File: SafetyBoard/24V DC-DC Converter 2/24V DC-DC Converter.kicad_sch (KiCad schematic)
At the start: 15 parts, among them J18 614004135023, U10 OKX-T/5-D12N-C

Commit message: hopefully this lets avadi pull
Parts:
- added C20: 1u, Capacitor_SMD:C_0805_2012Metric, symbol Device:C
- renumbered C27 to C16, C28 to C17, C18 to C21, C19 to C22, C29 to C23, C30 to C24, C31 to C25, C21 to C27, C26 to C32, J18 to J12, R58 to R53, R53 to R55, U10 to U9
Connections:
- net GND: now also C20.2
- net 5V: now reaches C16.1, C17.1, J12.1 (VBUS), U9.1 (+VOUT)
- net at FL1.3 (CASE): now also C20.1

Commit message: rough layout done
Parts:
- added F11, F12: ~, 0footprints:FUSE_3522-2, symbol Device:Fuse
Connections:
- net 12V_OUT: now also F11.2; no longer C27.1, C32.1, PS1.12 (VOUT_(+)_2), PS1.7 (SENSE+), PS1.8 (VOUT_(+)_1)
- net 5V: now also F12.2; no longer J12.1 (VBUS)
- new net: C27.1, C32.1, F11.1, PS1.12 (VOUT_(+)_2), PS1.7 (SENSE+), PS1.8 (VOUT_(+)_1)
- new net: F12.1, J12.1 (VBUS)
- no-connect marks 1 -> 3
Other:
- moved on the sheet: J12
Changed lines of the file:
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@@
+	)
+	(junction
+		(at 85.09 99.06)
+		(diameter 0)
+		(color 0 0 0 0)
 	)
 	(junction
@@
 	)
 	(junction
-		(at 85.09 99.06)
-		(diameter 0)
-		(color 0 0 0 0)
-	)
-	(junction
 		(at 153.67 46.99)
 		(diameter 0)
@@
 	)
 	(no_connect
+		(at 54.356 96.52)
+	)
+	(no_connect
+		(at 54.356 93.98)
+	)
+	(no_connect
 		(at 228.6 49.53)
 	)
@@
 	(wire
 		(pts
+			(xy 54.356 91.44) (xy 76.454 91.44)
+		)
+		(stroke
+			(width 0)
+			(type default)
+		)
+	)
+	(wire
+		(pts
 			(xy 144.78 39.37) (xy 151.13 39.37)
 		)
@@
 	(wire
 		(pts
+			(xy 264.16 39.37) (xy 268.986 39.37)
+		)
+		(stroke
+			(width 0)
+			(type default)
+		)
+	)
+	(wire
+		(pts
 			(xy 245.11 39.37) (xy 256.54 39.37)
 		)
@@
 	(wire
 		(pts
-			(xy 256.54 39.37) (xy 260.35 39.37)
-		)
-		(stroke
-			(width 0)
-			(type default)
-		)
-	)
-	(wire
-		(pts
 			(xy 232.41 54.61) (xy 232.41 52.07)
 		)
@@
 	(wire
 		(pts
+			(xy 68.58 99.06) (xy 54.356 99.06)
+		)
+		(stroke
+			(width 0)
+			(type default)
+		)
+	)
+	(wire
+		(pts
 			(xy 92.71 99.06) (xy 106.426 99.06)
 		)
@@
 	(wire
 		(pts
+			(xy 76.2 99.06) (xy 85.09 99.06)
+		)
+		(stroke
+			(width 0)
+			(type default)
+		)
+	)
+	(wire
+		(pts
 			(xy 153.67 49.53) (xy 153.67 46.99)
 		)
@@
 	(wire
 		(pts
-			(xy 76.454 99.06) (xy 85.09 99.06)
-		)
-		(stroke
-			(width 0)
-			(type default)
-		)
-	)
-	(wire
-		(pts
 			(xy 228.6 41.91) (xy 233.68 41.91)
 		)
@@
 		(pts
 			(xy 192.532 101.6) (xy 194.818 101.6)
+		)
+		(stroke
+			(width 0)
+			(type default)
+		)
+	)
+	(wire
+		(pts
+			(xy 54.356 88.9) (xy 76.454 88.9)
 		)
 		(stroke
@@
 	(hierarchical_label "12V_OUT"
 		(shape output)
-		(at 260.35 39.37 0)
+		(at 268.986 39.37 0)
 		(effects
 			(font
@@
 	(symbol
 		(lib_id "614004135023:614004135023")
-		(at 66.294 96.52 180)
+		(at 44.196 96.52 180)
 		(unit 1)
 		(exclude_from_sim no)
@@
 		(fields_autoplaced yes)
 		(property "Reference" "J12"
-			(at 65.5237 83.312 0)
+			(at 43.4257 83.312 0)
 			(effects
 				(font
@@
 		)
 		(property "Value" "614004135023"
-			(at 65.5237 85.852 0)
+			(at 43.4257 85.852 0)
 			(effects
 				(font
@@
 		)
 		(property "Footprint" "footprints:614004135023"
-			(at 66.294 96.52 0)
+			(at 44.196 96.52 0)
 			(effects
 				(font
@@
 		)
 		(property "Datasheet" ""
-			(at 66.294 96.52 0)
+			(at 44.196 96.52 0)
 			(effects
 				(font
@@
 		)
 		(property "Description" ""
-			(at 66.294 96.52 0)
+			(at 44.196 96.52 0)
 			(effects
 				(font
@@
 		)
 		(property "DigiKey_Part_Number" "732-2732-ND"
-			(at 66.294 96.52 0)
+			(at 44.196 96.52 0)
 			(effects
 				(font
@@
 		)
 		(property "SnapEDA_Link" "https://www.snapeda.com/parts/614004135023/Wurth+Electronics/view-part/?ref=snap"
-			(at 66.294 96.52 0)
+			(at 44.196 96.52 0)
 			(effects
 				(font
@@
 		)
 		(property "Description_1" "WR-COM_USB_Type A_Vertical_THT"
-			(at 66.294 96.52 0)
+			(at 44.196 96.52 0)
 			(effects
 				(font
@@
 		)
 		(property "MF" "Wurth Electronics"
-			(at 66.294 96.52 0)
+			(at 44.196 96.52 0)
 			(effects
 				(font
@@
 		)
 		(property "Package" "None"
-			(at 66.294 96.52 0)
+			(at 44.196 96.52 0)
 			(effects
 				(font
@@
 		)
 		(property "Check_prices" "https://www.snapeda.com/parts/614004135023/Wurth+Electronics/view-part/?ref=eda"
-			(at 66.294 96.52 0)
+			(at 44.196 96.52 0)
 			(effects
 				(font
@@
 		)
 		(property "MP" "614004135023"
-			(at 66.294 96.52 0)
+			(at 44.196 96.52 0)
 			(effects
 				(font
@@
 	)
 	(symbol
+		(lib_id "Device:Fuse")
+		(at 72.39 99.06 90)
+		(unit 1)
+		(exclude_from_sim no)
+		(in_bom yes)
+		(on_board yes)
+		(dnp no)
+		(property "Reference" "F12"
+			(at 72.39 96.774 90)
+			(effects
+				(font
+					(size 1.27 1.27)
+				)
+			)
+		)
+		(property "Value" "~"
+			(at 72.39 100.838 90)
+			(effects
+				(font
+					(size 1.27 1.27)
+				)
+			)
+		)
+		(property "Footprint" "0footprints:FUSE_3522-2"
+			(at 72.39 100.838 90)
+			(effects
+				(font
+					(size 1.27 1.27)
+				)
+				(hide yes)
+			)
+		)
+		(property "Datasheet" "https://www.keyelco.com/userAssets/file/M65p41.pdf"
+			(at 72.39 99.06 0)
+			(effects
+				(font
+					(size 1.27 1.27)
+				)
+				(hide yes)
+			)
+		)
+		(property "Description" "Fuse"
+			(at 72.39 99.06 0)
+			(effects
+				(font
+					(size 1.27 1.27)
+				)
+				(hide yes)
+			)
+		)
+		(pin "1"
+		)
+		(pin "2"
+		)
+		(instances
+			(project "SafetyBoard"
+				(path "/30d029c6-868b-41ac-953d-167a7d76c1a3/6fc2b78a-838b-45c0-bee7-c17fc640308b"
+					(reference "F12")
+					(unit 1)
+				)
+			)
+		)
+	)
+	(symbol
 		(lib_id "Device:C")
 		(at 184.658 105.41 0)
@@
 					(unit 1)
 				)
+			)
+		)
+	)
+	(symbol
+		(lib_id "Device:Fuse")
+		(at 260.35 39.37 90)
+		(unit 1)
+		(exclude_from_sim no)
+		(in_bom yes)
+		(on_board yes)
+		(dnp no)
+		(property "Reference" "F11"
+			(at 260.35 37.084 90)
+			(effects
+				(font
+					(size 1.27 1.27)
+				)
+			)
+		)
+		(property "Value" "~"
+			(at 260.35 41.148 90)
+			(effects
+				(font
+					(size 1.27 1.27)
+				)
+			)
+		)
+		(property "Footprint" "0footprints:FUSE_3522-2"
+			(at 260.35 41.148 90)
+			(effects
+				(font
+					(size 1.27 1.27)
+				)
+				(hide yes)
+			)
+		)
+		(property "Datasheet" "https://www.keyelco.com/userAssets/file/M65p41.pdf"
+			(at 260.35 39.37 0)
+			(effects
+				(font
+					(size 1.27 1.27)
+				)
+				(hide yes)
+			)
+		)
+		(property "Description" "Fuse"
+			(at 260.35 39.37 0)
+			(effects
+				(font
+					(size 1.27 1.27)
+				)
+				(hide yes)
+			)
+		)
+		(pin "1"
+		)
+		(pin "2"
+		)
+		(instances
+			(project "SafetyBoard"
+				(path "/30d029c6-868b-41ac-953d-167a7d76c1a3/6fc2b78a-838b-45c0-bee7-c17fc640308b"
+					(reference "F11")
+					(unit 1)
+				)

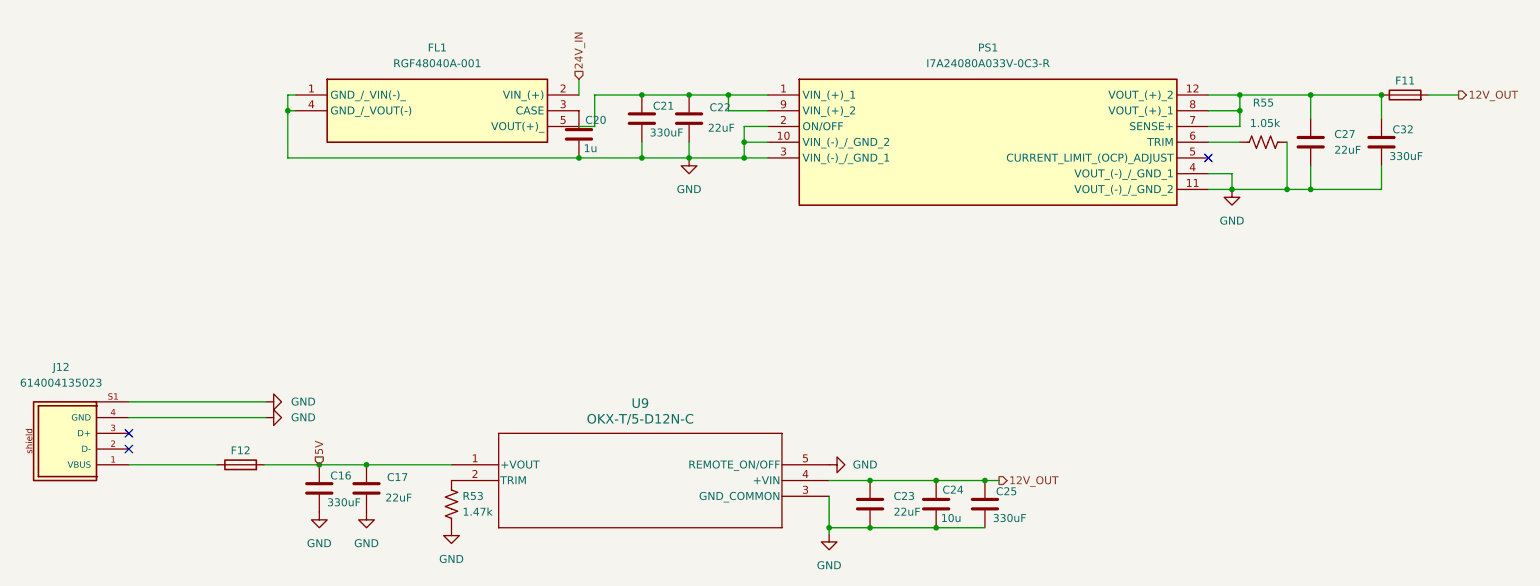
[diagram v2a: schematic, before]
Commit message: silkscreen and some fuses or something
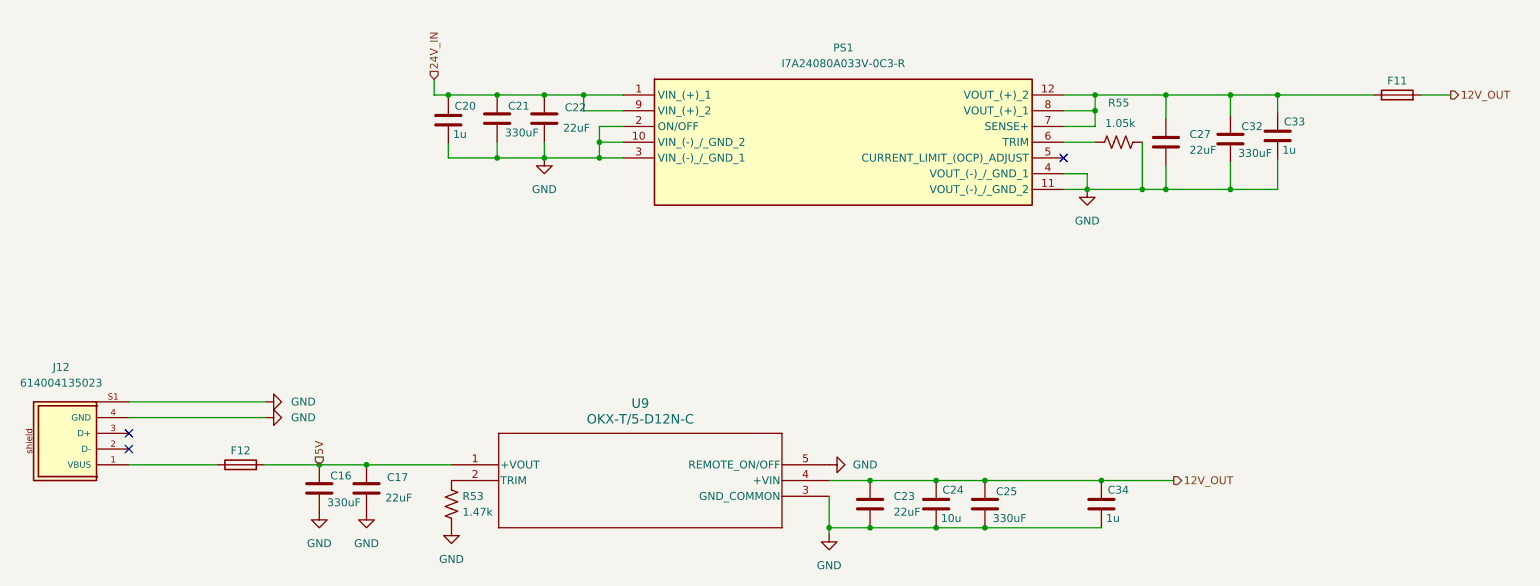
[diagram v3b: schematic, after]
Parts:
- removed FL1: RGF48040A-001, DCDCfootprints:EMI Filter RGF48040A001, symbol Filter:RGF48040A-001
- added C33, C34: 1u, Capacitor_SMD:C_0805_2012Metric, symbol Device:C
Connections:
- net 12V_OUT: now also C34.1
- net 24V_IN: now also C20.1, C21.1, C22.1, PS1.1 (VIN_(+)_1), PS1.9 (VIN_(+)_2)
- net GND: now also C33.2, C34.2
- net at C27.1, C32.1, F11.1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: now also C33.1
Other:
- moved on the sheet: C20, C21, C22, C27, C32, F11, PS1, R55

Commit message: I think think this is final but need to defuck the BOM
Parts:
- added R51: ~, Resistor_SMD:R_0805_2012Metric, symbol Device:R_US
- F11: renamed from F12; value ~ -> 3A
- renumbered C34 to C27, C27 to C28, C32 to C29, C33 to C30, F11 to F12, J12 to J13, R53 to R49, R55 to R52
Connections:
- net GND: now also R51.2
- net at PS1.5 (CURRENT_LIMIT_(OCP)_ADJUST): now also R51.1
- no-connect marks 3 -> 2
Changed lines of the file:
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@@
+	)
+	(junction
+		(at 212.852 54.61)
+		(diameter 0)
+		(color 0 0 0 0)
 	)
 	(junction
@@
 		(at 54.356 93.98)
 	)
-	(no_connect
-		(at 205.232 49.53)
-	)
 	(wire
 		(pts
@@
 	(wire
 		(pts
-			(xy 209.042 54.61) (xy 217.932 54.61)
+			(xy 209.042 54.61) (xy 212.852 54.61)
 		)
 		(stroke
@@
 	(wire
 		(pts
+			(xy 212.852 54.61) (xy 217.932 54.61)
+		)
+		(stroke
+			(width 0)
+			(type default)
+		)
+	)
+	(wire
+		(pts
 			(xy 54.356 91.44) (xy 76.454 91.44)
 		)
@@
 		(pts
 			(xy 92.71 99.06) (xy 106.426 99.06)
+		)
+		(stroke
+			(width 0)
+			(type default)
+		)
+	)
+	(wire
+		(pts
+			(xy 212.852 49.53) (xy 212.852 54.61)
 		)
 		(stroke
@@
 		(dnp no)
 		(fields_autoplaced yes)
-		(property "Reference" "C27"
+		(property "Reference" "C28"
 			(at 225.552 45.7199 0)
 			(effects
@@
 			(project ""
 				(path "/30d029c6-868b-41ac-953d-167a7d76c1a3/6fc2b78a-838b-45c0-bee7-c17fc640308b"
-					(reference "C27")
+					(reference "C28")
 					(unit 1)
 				)
@@
 		(on_board yes)
 		(dnp no)
-		(property "Reference" "R55"
+		(property "Reference" "R52"
 			(at 214.122 40.64 90)
 			(effects
@@
 			(project ""
 				(path "/30d029c6-868b-41ac-953d-167a7d76c1a3/6fc2b78a-838b-45c0-bee7-c17fc640308b"
-					(reference "R55")
+					(reference "R52")
 					(unit 1)
 				)
@@
 		(on_board yes)
 		(dnp no)
-		(property "Reference" "R53"
+		(property "Reference" "R49"
 			(at 108.204 104.1399 0)
 			(effects
@@
 			(project ""
 				(path "/30d029c6-868b-41ac-953d-167a7d76c1a3/6fc2b78a-838b-45c0-bee7-c17fc640308b"
-					(reference "R53")
+					(reference "R49")
 					(unit 1)
 				)
@@
 		(dnp no)
 		(fields_autoplaced yes)
-		(property "Reference" "#PWR090"
+		(property "Reference" "#PWR092"
 			(at 82.804 91.44 0)
 			(effects
@@
 			(project "SafetyBoard"
 				(path "/30d029c6-868b-41ac-953d-167a7d76c1a3/6fc2b78a-838b-45c0-bee7-c17fc640308b"
-					(reference "#PWR090")
+					(reference "#PWR092")
 					(unit 1)
 				)
@@
 		(dnp no)
 		(fields_autoplaced yes)
-		(property "Reference" "J12"
+		(property "Reference" "J13"
 			(at 43.4257 83.312 0)
 			(effects
@@
 			(project ""
 				(path "/30d029c6-868b-41ac-953d-167a7d76c1a3/6fc2b78a-838b-45c0-bee7-c17fc640308b"
-					(reference "J12")
+					(reference "J13")
 					(unit 1)
 				)
@@
 		(on_board yes)
 		(dnp no)
-		(property "Reference" "C34"
+		(property "Reference" "C27"
 			(at 212.344 103.124 0)
 			(effects
@@
 			(project "SafetyBoard"
 				(path "/30d029c6-868b-41ac-953d-167a7d76c1a3/6fc2b78a-838b-45c0-bee7-c17fc640308b"
-					(reference "C34")
+					(reference "C27")
 					(unit 1)
 				)
@@
 		(on_board yes)
 		(dnp no)
-		(property "Reference" "C33"
+		(property "Reference" "C30"
 			(at 240.792 43.688 0)
 			(effects
@@
 			(project "SafetyBoard"
 				(path "/30d029c6-868b-41ac-953d-167a7d76c1a3/6fc2b78a-838b-45c0-bee7-c17fc640308b"
-					(reference "C33")
+					(reference "C30")
 					(unit 1)
 				)
@@
 		(dnp no)
 		(fields_autoplaced yes)
-		(property "Reference" "#PWR093"
+		(property "Reference" "#PWR095"
 			(at 106.426 115.57 0)
 			(effects
@@
 			(project "SafetyBoard"
 				(path "/30d029c6-868b-41ac-953d-167a7d76c1a3/6fc2b78a-838b-45c0-bee7-c17fc640308b"
-					(reference "#PWR093")
+					(reference "#PWR095")
 					(unit 1)
 				)
@@
 		(on_board yes)
 		(dnp no)
-		(property "Reference" "C32"
+		(property "Reference" "C29"
 			(at 233.934 44.45 0)
 			(effects
@@
 			(project "SafetyBoard"
 				(path "/30d029c6-868b-41ac-953d-167a7d76c1a3/6fc2b78a-838b-45c0-bee7-c17fc640308b"
-					(reference "C32")
+					(reference "C29")
 					(unit 1)
 				)
@@
 		(on_board yes)
 		(dnp no)
-		(property "Reference" "F12"
+		(property "Reference" "F11"
 			(at 72.39 96.774 90)
 			(effects
@@
 			)
 		)
-		(property "Value" "~"
+		(property "Value" "3A"
 			(at 72.39 100.838 90)
 			(effects
@@
 			(project "SafetyBoard"
 				(path "/30d029c6-868b-41ac-953d-167a7d76c1a3/6fc2b78a-838b-45c0-bee7-c17fc640308b"
-					(reference "F12")
+					(reference "F11")
 					(unit 1)
 				)
@@
 		(dnp no)
 		(fields_autoplaced yes)
-		(property "Reference" "#PWR089"
+		(property "Reference" "#PWR091"
 			(at 82.804 88.9 0)
 			(effects
@@
 			(project "SafetyBoard"
 				(path "/30d029c6-868b-41ac-953d-167a7d76c1a3/6fc2b78a-838b-45c0-bee7-c17fc640308b"
-					(reference "#PWR089")
+					(reference "#PWR091")
 					(unit 1)
 				)
@@
 		(dnp no)
 		(fields_autoplaced yes)
-		(property "Reference" "#PWR096"
+		(property "Reference" "#PWR097"
 			(at 173.736 99.06 0)
 			(effects
@@
 			(project "SafetyBoard"
 				(path "/30d029c6-868b-41ac-953d-167a7d76c1a3/6fc2b78a-838b-45c0-bee7-c17fc640308b"
-					(reference "#PWR096")
+					(reference "#PWR097")
 					(unit 1)
 				)
@@
 		(dnp no)
 		(fields_autoplaced yes)
-		(property "Reference" "#PWR098"
+		(property "Reference" "#PWR0100"
 			(at 209.042 60.96 0)
 			(effects
@@
 			(project "SafetyBoard"
 				(path "/30d029c6-868b-41ac-953d-167a7d76c1a3/6fc2b78a-838b-45c0-bee7-c17fc640308b"
-					(reference "#PWR098")
+					(reference "#PWR0100")
 					(unit 1)
 				)
@@
 		(dnp no)
 		(fields_autoplaced yes)
-		(property "Reference" "#PWR094"
+		(property "Reference" "#PWR096"
 			(at 121.412 55.88 0)
 			(effects
@@
 			(project ""
 				(path "/30d029c6-868b-41ac-953d-167a7d76c1a3/6fc2b78a-838b-45c0-bee7-c17fc640308b"
-					(reference "#PWR094")
+					(reference "#PWR096")
 					(unit 1)
 				)
@@
 		(on_board yes)
 		(dnp no)
-		(property "Reference" "F11"
+		(property "Reference" "F12"
 			(at 259.08 37.084 90)
 			(effects
@@
 			(project "SafetyBoard"
 				(path "/30d029c6-868b-41ac-953d-167a7d76c1a3/6fc2b78a-838b-45c0-bee7-c17fc640308b"
-					(reference "F11")
+					(reference "F12")
 					(unit 1)
 				)
@@
 		(dnp no)
 		(fields_autoplaced yes)
-		(property "Reference" "#PWR097"
+		(property "Reference" "#PWR098"
 			(at 167.386 116.586 0)
 			(effects
@@
 			(project ""
 				(path "/30d029c6-868b-41ac-953d-167a7d76c1a3/6fc2b78a-838b-45c0-bee7-c17fc640308b"
-					(reference "#PWR097")
+					(reference "#PWR098")
 					(unit 1)
 				)
@@
 		(dnp no)
 		(fields_autoplaced yes)
-		(property "Reference" "#PWR092"
+		(property "Reference" "#PWR094"
 			(at 92.71 113.03 0)
 			(effects
@@
 			(project "SafetyBoard"
 				(path "/30d029c6-868b-41ac-953d-167a7d76c1a3/6fc2b78a-838b-45c0-bee7-c17fc640308b"
-					(reference "#PWR092")
+					(reference "#PWR094")
 					(unit 1)
 				)
@@
 		(dnp no)
 		(fields_autoplaced yes)
-		(property "Reference" "#PWR091"
+		(property "Reference" "#PWR093"
 			(at 85.09 113.03 0)
 			(effects
@@
 			(project "SafetyBoard"
 				(path "/30d029c6-868b-41ac-953d-167a7d76c1a3/6fc2b78a-838b-45c0-bee7-c17fc640308b"
-					(reference "#PWR091")
-					(unit 1)
-				)
+					(reference "#PWR093")
+					(unit 1)
+				)
+			)
+		)
+	)
+	(symbol
+		(lib_id "Device:R_US")
+		(at 209.042 49.53 90)
+		(unit 1)
+		(exclude_from_sim no)
+		(in_bom yes)
+		(on_board yes)
+		(dnp no)
+		(property "Reference" "R51"
+			(at 209.042 43.18 90)
+			(effects
+				(font
+					(size 1.27 1.27)
+				)
+			)
+		)
+		(property "Value" "~"
+			(at 209.296 46.482 90)
+			(effects
+				(font
+					(size 1.27 1.27)
+				)
+			)
+		)
+		(property "Footprint" "Resistor_SMD:R_0805_2012Metric"
+			(at 209.296 48.514 90)
+			(effects
+				(font
+					(size 1.27 1.27)
+				)
+				(hide yes)
+			)
+		)
+		(property "Datasheet" "~"
+			(at 209.042 49.53 0)
+			(effects
+				(font
+					(size 1.27 1.27)
+				)
+				(hide yes)
+			)
+		)
+		(property "Description" "Resistor, US symbol"
+			(at 209.042 49.53 0)
+			(effects
+				(font
+					(size 1.27 1.27)
+				)
+				(hide yes)
+			)
+		)
+		(pin "1"
+		)
+		(pin "2"
+		)
+		(instances
+			(project "SafetyBoard"
+				(path "/30d029c6-868b-41ac-953d-167a7d76c1a3/6fc2b78a-838b-45c0-bee7-c17fc640308b"
+					(reference "R51")
+					(unit 1)
+				)

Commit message: Safety Board: added BOM and updated schematics
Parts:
- C16, C21, C25, C29: MFG (none) -> Panasonic Electronic Components; MPN (none) -> 16SVPK330M
- C17, C22, C23, C28: MFG (none) -> Murata; MPN (none) -> GRM21BR61A226ME44L
- C20, C27, C30: value 1u -> 1uF
- C24: value 10u -> 10uF
- F11, F12: MFG (none) -> Littelfuse; MPN (none) -> 01530007Z
- J13: MFG (none) -> Wurth Elektronik; MPN (none) -> 614004135023
- PS1: MFG (none) -> TDK-Lambda; MPN (none) -> I7A24080A033V-0C3-R
- R52: MFG (none) -> Stackpole Electronics Inc; MPN (none) -> RNCF0805DKE1K05
- U9: MFG (none) -> Murata Power Solutions; MPN (none) -> OKX-T/5-D12N-C

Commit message: updates I think
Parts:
- added C35: 22uf, Capacitor_SMD:C_2220_5750Metric_Pad1.97x5.40mm_HandSolder, symbol Device:C
- C16, C25, C29: value 330uF -> 22uf; MFG Panasonic Electronic Components -> TDK; MPN 16SVPK330M -> C5750X7R1E226M250KA
- C21: footprint Capacitor_SMD:C_2220_5750Metric_Pad1.97x5.40mm_HandSolder -> Capacitor_THT:CP_Radial_D12.5mm_P5.00mm
- C23, C28: value 22uF -> 22uf; footprint Capacitor_SMD:C_0805_2012Metric -> Capacitor_SMD:C_2220_5750Metric_Pad1.97x5.40mm_HandSolder; MFG Murata -> TDK; MPN GRM21BR61A226ME44L -> C5750X7R1E226M250KA
- F11: value 3A -> 3A MAX; MFG Littelfuse -> Keystone Electronics; MPN 01530007Z -> 3522-2
- F12: MFG Littelfuse -> Keystone Electronics; MPN 01530007Z -> 3522-2
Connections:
- net 12V_OUT: no longer C25.1
- net GND: now also C35.2
- net at C28.1, C29.1, C30.1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: now also C25.1, C35.1
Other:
- moved on the sheet: C30

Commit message: silkscreen finish touches
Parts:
- C21: MFG Panasonic Electronic Components -> TDK; MPN 16SVPK330M -> B41866C6337M000
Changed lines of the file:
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@@
 			)
 		)
-		(property "MFG" "Panasonic Electronic Components"
+		(property "MFG" "TDK "
 			(at 113.792 43.18 0)
 			(effects
@@
 			)
 		)
-		(property "MPN" "16SVPK330M"
+		(property "MPN" "B41866C6337M000 "
 			(at 113.792 43.18 0)
 			(effects
